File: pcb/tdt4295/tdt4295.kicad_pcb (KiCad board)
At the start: 6 copper layers, 183 parts, among them J101 ARM 20 Pin Debug Header, J102 MCU USART1 Header, J103 DM1AA-SF-PEJ(21), J104 MCU GPIO Header, J301 FPGA__debug, J501 618015330923, J502 FPGA GPIO, P201 690-005-299-043, U101 EFM32GG12B810F1024GQ64, U102 COM-09032 Joystick, U103 COM-09032 Joystick, U201 PHDMI2AB4, U202 TPS54294, U203 TPS54294, U301 S25FL127SABMFV101, U302 NUP4114UCW1T2G, U303 XC7A100T-FTG256-tdt4295, U501 NUP4114UCW1T2G, U502 NUP4114UCW1T2G, U503 NUP4114UCW1T2G, U504 NUP4114UCW1T2G, U601 DSC1001AL5-100.0000, Y101 48MHz

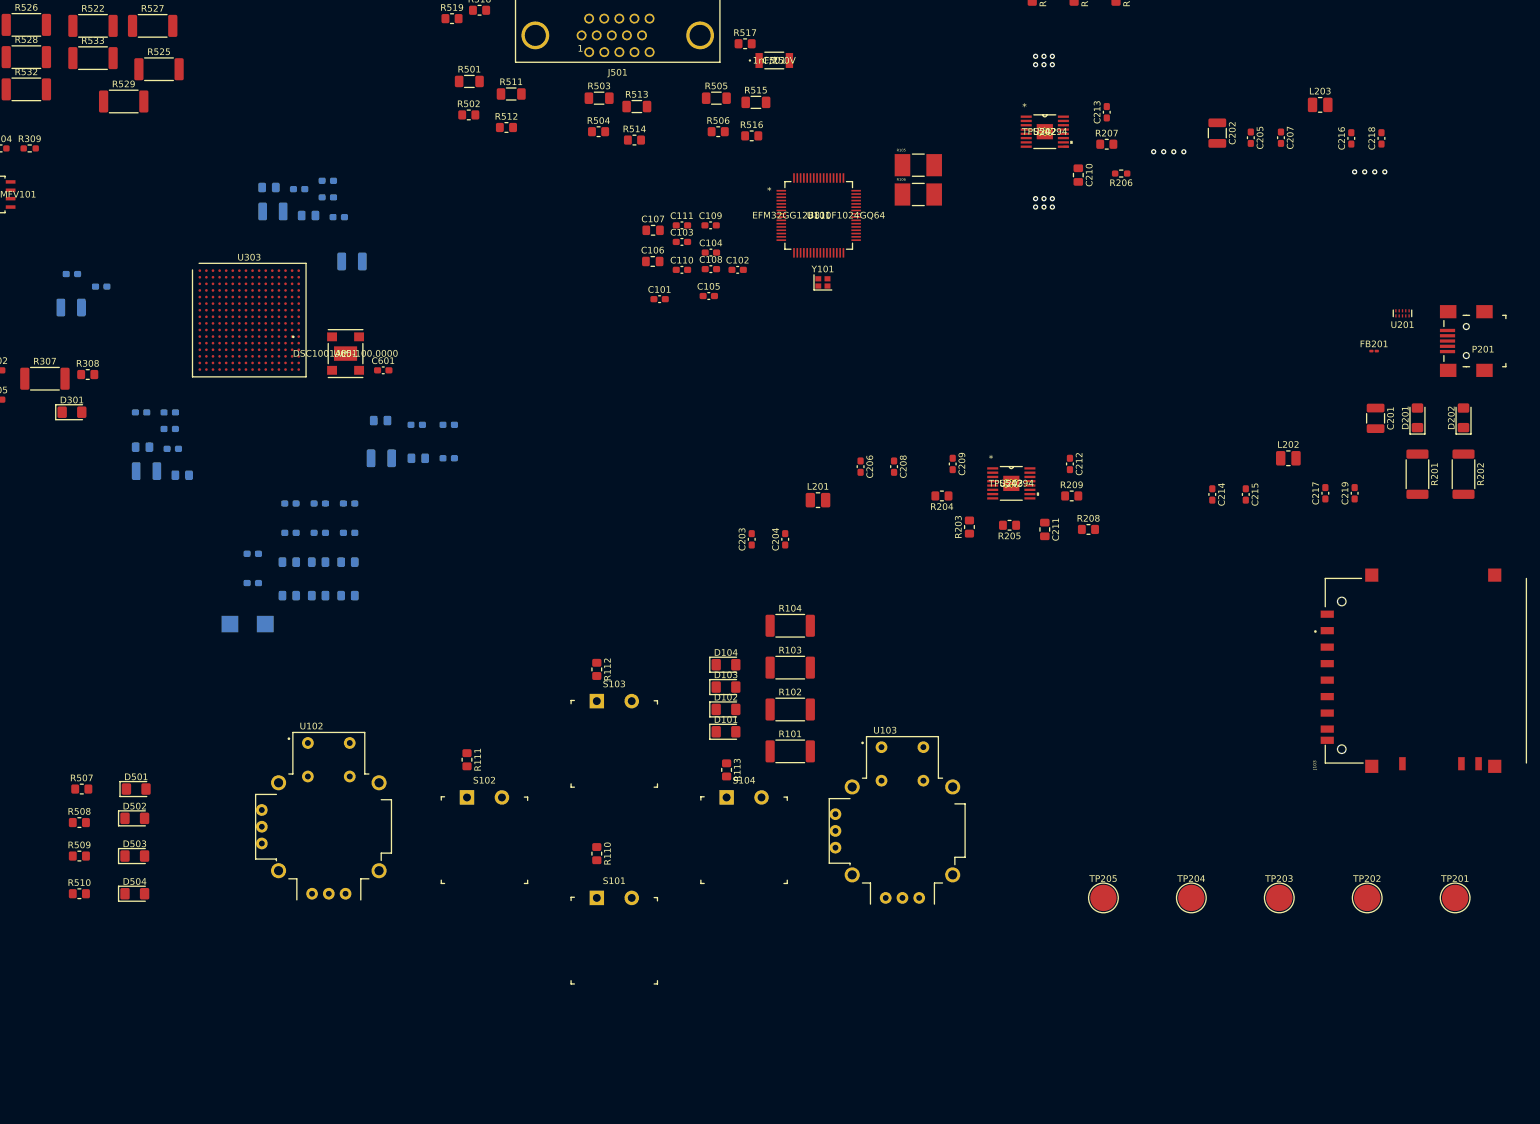
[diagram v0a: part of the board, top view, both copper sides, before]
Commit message: add thermal relief zoning for both voltage regulators
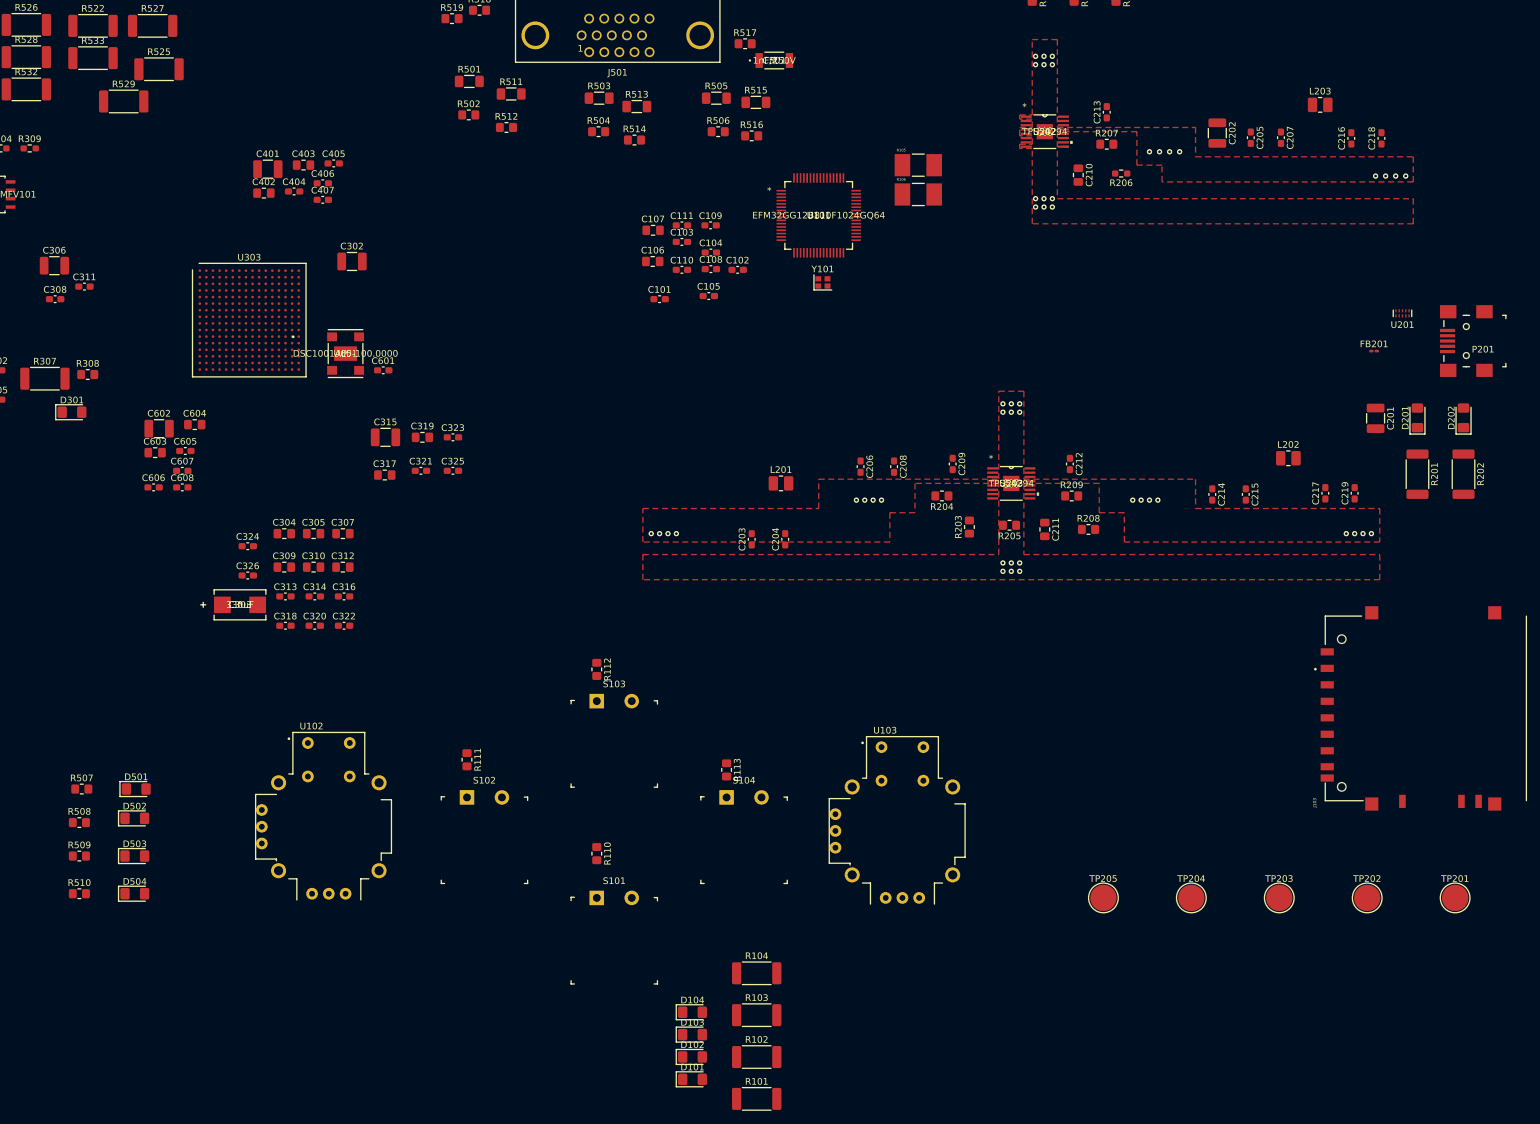
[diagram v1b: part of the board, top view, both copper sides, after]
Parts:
- C302, C303, C304, C305, C306, C307, C308, C309, C310, C311, C312, C313, C314, C315, C316, C317, C318, C319, C320, C321, C322, C323, C324, C325, C326, C401, C402, C403, C404, C405, C406, C407, C602, C603, C604, C605, C606, C607, C608: moved to F.Cu
- moved D102 52.9 mm to (157.4, 184.8)
- moved R104 52.9 mm to (167.1, 172.1)
- moved D104 52.9 mm to (157.4, 178.0)
- moved R103 52.9 mm to (167.1, 178.4)
- moved D101 52.9 mm to (157.4, 188.2)
- moved D103 52.9 mm to (157.4, 181.4)
- moved R101 52.9 mm to (167.1, 191.1)
- moved R102 52.9 mm to (167.1, 184.8)
- moved C318 18.6 mm to (95.7, 119.4)
- moved C320 18.6 mm to (100.1, 119.4)
- moved C322 18.6 mm to (104.5, 119.4)
- moved C606 11.5 mm to (75.7, 98.4)
- moved C608 11.5 mm to (80.0, 98.4)
- moved C313 9.68 mm to (95.7, 114.9)
- moved C314 9.68 mm to (100.1, 114.9)
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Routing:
- net (no net): track 37.1 -> 6.94 mm, vias 14 -> 42
- net GND: track 16.5 -> 0.00 mm
- added copper zone on F.Cu, net GND
- removed copper zone on In2.Cu, net GND
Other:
- net class Default: trace_width 0.3 -> 0.2
- net class Power: trace_width 0.5 -> 0.3

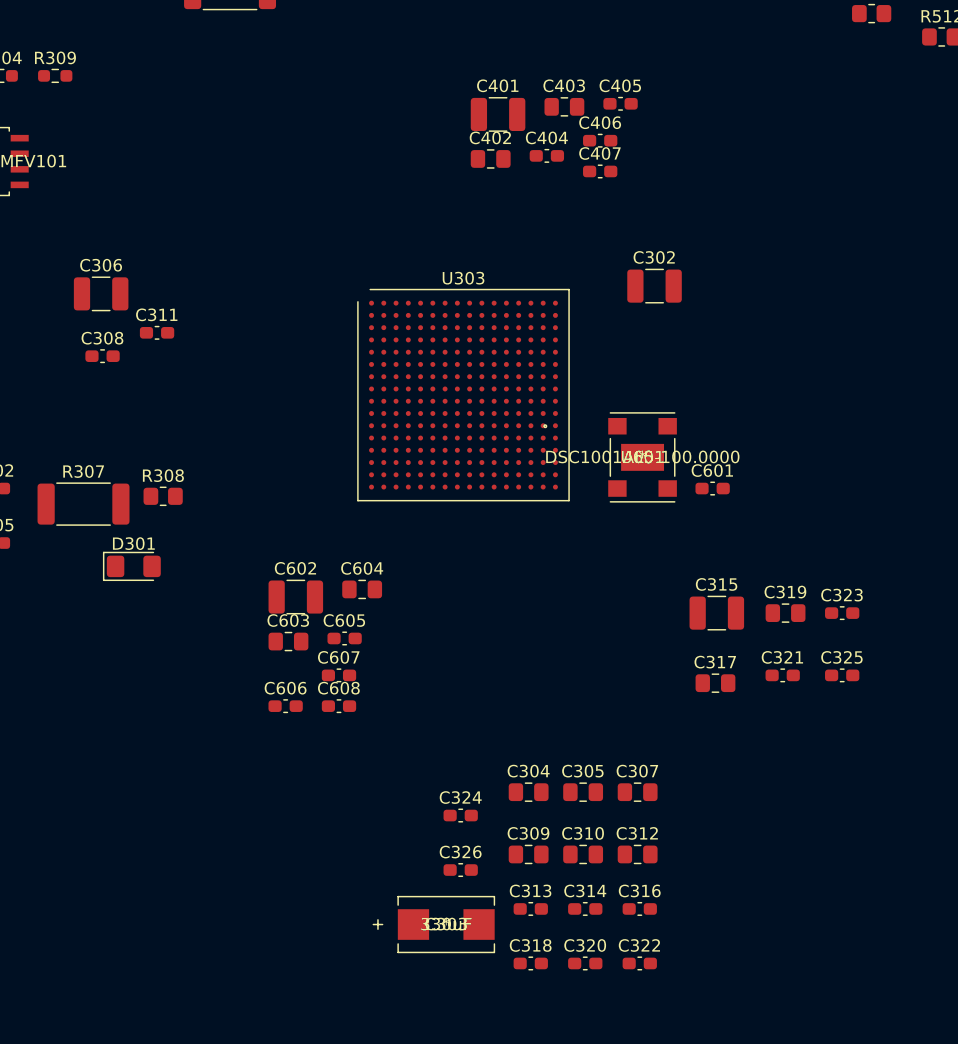
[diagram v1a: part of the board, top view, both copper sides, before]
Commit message: start routing pins out from FPGA
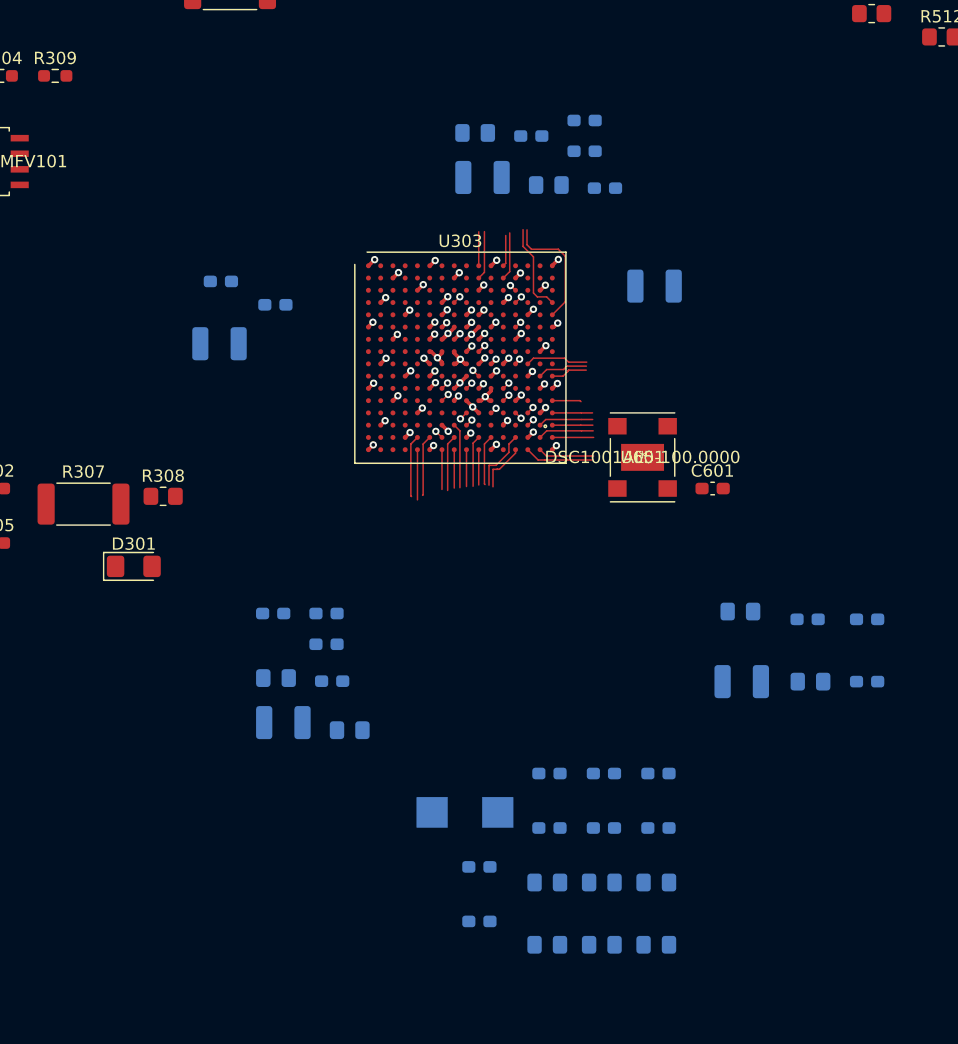
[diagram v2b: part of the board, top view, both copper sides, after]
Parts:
- C302, C303, C304, C305, C306, C307, C308, C309, C310, C311, C312, C313, C314, C315, C316, C317, C318, C319, C320, C321, C322, C323, C324, C325, C326, C401, C402, C403, C404, C405, C406, C407, C602, C603, C604, C605, C606, C607, C608: moved to B.Cu
- moved C318 15.6 mm to (97.2, 103.9)
- moved C320 15.6 mm to (101.6, 103.9)
- moved C322 15.6 mm to (106.1, 103.9)
- moved C304 12.5 mm to (97.0, 117.9)
- moved C305 12.5 mm to (101.5, 117.9)
- moved C307 12.5 mm to (105.9, 117.9)
- moved C604 11.5 mm to (80.9, 100.4)
- moved C308 11.4 mm to (70.4, 63.8)
- moved C306 10.5 mm to (70.3, 68.8)
- moved C602 10.3 mm to (75.5, 99.7)
- moved C311 9.92 mm to (74.8, 65.7)
- moved C303 9.27 mm to (90.3, 107.1)
- moved C324 8.77 mm to (91.5, 116.0)
- moved C606 7.63 mm to (74.6, 90.8)
- moved C608 7.63 mm to (79.0, 90.8)
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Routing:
- net GND: track 0.00 -> 30.9 mm, vias 6 -> 46
- net FPGA_PROGRAM_B: track 0.00 -> 22.5 mm, vias 0 -> 1
- net Net-(R305-Pad2): track 0.00 -> 14.4 mm, vias 0 -> 1
- net /FPGA/TMS_JTAG: track 0.00 -> 11.5 mm, vias 0 -> 1
- net /FPGA/TCK_JTAG: track 0.00 -> 11.3 mm, vias 0 -> 1
- net FPGA_MCU_GPIO_2: track 0.00 -> 9.94 mm
- net +3V3: track 0.00 -> 9.76 mm, vias 0 -> 14
- net FPGA_EXT_IO11: track 0.00 -> 8.38 mm, vias 0 -> 1
- net FPGA_MCU_GPIO_1: track 0.00 -> 8.11 mm, vias 0 -> 1
- net FPGA_EXT_IO0: track 0.00 -> 7.84 mm, vias 0 -> 1
- net /FPGA/IOB14/QSPI_CS: track 0.00 -> 7.39 mm, vias 0 -> 1
- net FPGA_MCU_GPIO_3: track 0.00 -> 7.38 mm
- net VGA_B1: track 0.00 -> 7.33 mm, vias 0 -> 1
- net FPGA_EXT_IO12: track 0.00 -> 7.13 mm, vias 0 -> 1
- net FPGA_MCU_USART_CTS: track 0.00 -> 6.87 mm, vias 0 -> 1
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- added copper zone on In1.Cu, net +3V3

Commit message: do a minimal amount of routing for the 2nd power regulator
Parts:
- C209, C211, C212, R205: moved to B.Cu
- moved J103 53.5 mm to (317.8, 153.7)
- moved P201 38.2 mm to (312.8, 78.7)
- moved C201 38.2 mm to (299.1, 90.5)
- moved R201 34.3 mm to (288.9, 123.1)
- moved TP202 32.1 mm to (274.3, 189.2)
- moved TP203 32.1 mm to (261.0, 189.2)
- moved TP204 32.1 mm to (247.7, 189.2)
- moved TP205 32.1 mm to (234.3, 189.2)
- moved TP201 32.1 mm to (287.7, 189.2)
- moved U201 31.3 mm to (296.2, 68.6), turned to 180 degrees
- moved D201 31.1 mm to (288.9, 110.3)
- moved C203 27.9 mm to (139.7, 98.0)
- moved FB201 27.2 mm to (287.9, 80.3)
- moved R202 26.9 mm to (278.1, 123.1)
- moved C204 24.3 mm to (148.6, 98.0)
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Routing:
- net +5V: track 0.00 -> 182.5 mm, vias 0 -> 3
- net GND: track 30.9 -> 193.8 mm, vias 46 -> 88
- net +3V3: track 9.76 -> 105.1 mm
- net +1V8: track 3.20 -> 78.1 mm
- net Net-(C212-Pad2): track 0.00 -> 51.4 mm, vias 0 -> 2
- net Net-(C209-Pad2): track 0.00 -> 49.0 mm, vias 0 -> 2
- net Net-(C201-Pad1): track 0.00 -> 45.3 mm, vias 0 -> 2
- net Net-(R205-Pad2): track 0.00 -> 32.6 mm, vias 0 -> 3
- net Net-(R208-Pad2): track 0.00 -> 32.0 mm
- net Net-(R203-Pad2): track 0.00 -> 30.0 mm
- net USB_D+: track 0.00 -> 25.5 mm
- net USB_D-: track 0.00 -> 17.7 mm
- net Net-(C211-Pad1): track 0.00 -> 15.0 mm, vias 0 -> 1
- net Net-(C212-Pad1): track 0.00 -> 9.34 mm, vias 0 -> 1
- net Net-(D201-Pad1): track 0.00 -> 8.25 mm
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- added copper zone on +PWR, net +3V3
- added copper zone on +PWR, net +5V
- added copper zone on GND, net GND
- removed copper zone on In1.Cu, net +1V0
- removed copper zone on In1.Cu, net +3V3
- removed copper zone on In1.Cu, net +5V
